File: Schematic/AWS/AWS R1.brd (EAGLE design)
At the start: 50 x 70 mm, 23 parts, among them U1 SN754410_NE_16

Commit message: Modified Board
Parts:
- added U$3: PTC, GeekAmmo:MC331XX
- moved J4 45.4 mm to (45.7, 58.4), flipped to the bottom
- moved J5 41.9 mm to (45.7, 48.3), flipped to the bottom
- moved J2 40.6 mm to (45.7, 27.9), flipped to the bottom
- moved J3 40.6 mm to (45.7, 17.8), flipped to the bottom
- moved J8 38.4 mm to (7.62, 27.9), flipped to the bottom
- moved J6 35.6 mm to (7.62, 61.0), flipped to the bottom
- moved D1 31.0 mm to (35.6, 58.4)
- moved R6 28.4 mm to (40.6, 25.4), turned to 270 degrees
- moved R8 25.9 mm to (15.2, 7.62), turned to 0 degrees
- moved R9 25.9 mm to (15.2, 10.2), turned to 0 degrees
- moved R1 25.4 mm to (12.7, 53.3)
- moved R2 20.5 mm to (15.2, 45.7), turned to 90 degrees
- moved C1 20.3 mm to (15.2, 62.2)
- moved D2 16.1 mm to (17.8, 50.8)
- moved R7 16.1 mm to (33.0, 17.8), turned to 0 degrees
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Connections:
- new net N$4: J4.1, U$3.P$2
- net 12V: now also U$3.P$1; no longer J4.1
- net 5V: now also J6.2; no longer J6.1
- net GND: now also J3.2, J6.1; no longer J3.1, J6.2
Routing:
- net A2: track 58.4 -> 3.59 mm
- net D1: track 30.5 -> 0.00 mm
- net D3: track 27.9 -> 5.08 mm
- net D6: track 0.00 -> 22.9 mm
- net GND: track 188.3 -> 173.0 mm
- net A1: track 2.54 -> 17.8 mm
- net A0: track 2.54 -> 17.8 mm
- net N$1: track 5.16 -> 17.9 mm
- net D4: track 12.7 -> 0.00 mm
- net A7: track 19.1 -> 7.62 mm
- net A6: track 10.2 -> 20.3 mm
- net N$4: track 0.00 -> 7.77 mm
- net SOL-: track 20.3 -> 15.2 mm
- net N$2: track 10.2 -> 7.62 mm
- net 12V: track 91.5 -> 89.0 mm
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
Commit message: final
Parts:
- moved R5 11.4 mm to (33.0, 15.2), turned to 180 degrees
- moved R6 9.16 mm to (35.6, 17.8), turned to 180 degrees
- moved R7 5.08 mm to (33.0, 12.7), flipped to the bottom
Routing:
- net GND: track 173.0 -> 216.2 mm
- net D3: track 5.08 -> 38.1 mm
- net 12V: track 89.0 -> 104.2 mm
- net N$2: track 7.62 -> 15.2 mm
- net D6: track 22.9 -> 27.9 mm
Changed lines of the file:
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@@
 <element name="R3" library="SparkFun-Resistors" package="AXIAL-0.4" value="10k" x="33.02" y="27.94" rot="R90"/>
 <element name="R4" library="SparkFun-Resistors" package="AXIAL-0.4" value="3.3k" x="30.48" y="30.48" rot="R270"/>
-<element name="R5" library="SparkFun-Resistors" package="AXIAL-0.4" value="10k" x="38.1" y="25.4" rot="R270"/>
-<element name="R6" library="SparkFun-Resistors" package="AXIAL-0.4" value="10k" x="40.64" y="25.4" rot="R270"/>
-<element name="R7" library="SparkFun-Resistors" package="AXIAL-0.4" value="3.3k" x="33.02" y="17.78"/>
+<element name="R5" library="SparkFun-Resistors" package="AXIAL-0.4" value="10k" x="33.02" y="15.24" rot="R180"/>
+<element name="R6" library="SparkFun-Resistors" package="AXIAL-0.4" value="10k" x="35.56" y="17.78" rot="R180"/>
+<element name="R7" library="SparkFun-Resistors" package="AXIAL-0.4" value="3.3k" x="33.02" y="12.7" rot="MR0"/>
 <element name="R8" library="SparkFun-Resistors" package="AXIAL-0.4" value="330" x="15.24" y="7.62"/>
 <element name="R9" library="SparkFun-Resistors" package="AXIAL-0.4" value="56k" x="15.24" y="10.16"/>
@@
 <wire x1="40.64" y1="50.8" x2="40.64" y2="53.34" width="0.4064" layer="1"/>
 <wire x1="40.64" y1="53.34" x2="38.1" y2="53.34" width="0.4064" layer="1"/>
-<wire x1="38.1" y1="30.48" x2="38.1" y2="33.02" width="0.4064" layer="1"/>
+<wire x1="38.1" y1="15.24" x2="38.1" y2="33.02" width="0.4064" layer="1"/>
 </signal>
 <signal name="GND">
@@
 <wire x1="22.86" y1="45.72" x2="20.32" y2="45.72" width="0.4064" layer="1"/>
 <wire x1="20.32" y1="48.26" x2="22.86" y2="48.26" width="0.4064" layer="1"/>
-<wire x1="48.26" y1="53.34" x2="48.26" y2="38.1" width="0.4064" layer="1"/>
+<wire x1="48.26" y1="53.34" x2="48.26" y2="45.72" width="0.4064" layer="1"/>
+<wire x1="48.26" y1="45.72" x2="48.26" y2="38.1" width="0.4064" layer="1"/>
 <wire x1="48.26" y1="38.1" x2="35.56" y2="38.1" width="0.4064" layer="1"/>
 <wire x1="35.56" y1="38.1" x2="35.56" y2="35.56" width="0.4064" layer="1"/>
@@
 <wire x1="20.32" y1="45.72" x2="17.78" y2="45.72" width="0.4064" layer="1"/>
 <wire x1="30.48" y1="35.56" x2="35.56" y2="35.56" width="0.4064" layer="1"/>
-<wire x1="48.26" y1="17.78" x2="48.26" y2="38.1" width="0.4064" layer="1"/>
+<wire x1="48.26" y1="22.86" x2="48.26" y2="38.1" width="0.4064" layer="1"/>
 <contactref element="J3" pad="2"/>
+<wire x1="48.26" y1="22.86" x2="45.72" y2="22.86" width="0.4064" layer="1"/>
+<wire x1="45.72" y1="22.86" x2="45.72" y2="22.78" width="0.4064" layer="1"/>
+<wire x1="38.1" y1="12.7" x2="48.26" y2="12.7" width="0.4064" layer="1"/>
+<wire x1="48.26" y1="12.7" x2="48.26" y2="22.86" width="0.4064" layer="1"/>
+<wire x1="27.94" y1="45.72" x2="27.94" y2="48.26" width="0.4064" layer="1"/>
+<wire x1="27.94" y1="48.26" x2="40.64" y2="48.26" width="0.4064" layer="1"/>
+<wire x1="40.64" y1="48.26" x2="40.64" y2="45.72" width="0.4064" layer="1"/>
+<wire x1="40.64" y1="45.72" x2="48.26" y2="45.72" width="0.4064" layer="1"/>
 <wire x1="48.26" y1="38.1" x2="45.72" y2="38.18" width="0" layer="19" extent="1-1"/>
 <wire x1="17.78" y1="63.5" x2="22.86" y2="63.5" width="0" layer="19" extent="1-16"/>
 <wire x1="15.24" y1="63.5" x2="17.78" y2="63.5" width="0" layer="19" extent="16-16"/>
-<wire x1="27.94" y1="48.26" x2="22.86" y2="48.26" width="0" layer="19" extent="1-1"/>
-<wire x1="27.94" y1="45.72" x2="27.94" y2="48.26" width="0" layer="19" extent="1-1"/>
-<wire x1="45.72" y1="22.78" x2="48.26" y2="17.78" width="0" layer="19" extent="1-1"/>
-<wire x1="27.94" y1="17.78" x2="30.48" y2="35.56" width="0" layer="19" extent="1-1"/>
-<wire x1="27.94" y1="5.08" x2="27.94" y2="17.78" width="0" layer="19" extent="1-1"/>
+<wire x1="27.94" y1="5.08" x2="38.1" y2="12.7" width="0" layer="19" extent="1-1"/>
 </signal>
 <signal name="5V">
@@
 <contactref element="R7" pad="P$2"/>
 <contactref element="U$1" pad="D3"/>
-<wire x1="15.24" y1="30.48" x2="38.1" y2="17.78" width="0" layer="19" extent="1-1"/>
-<wire x1="40.64" y1="20.32" x2="38.1" y2="20.32" width="0.4064" layer="1"/>
-<wire x1="38.1" y1="20.32" x2="38.1" y2="17.78" width="0.4064" layer="1"/>
+<wire x1="30.48" y1="17.78" x2="27.94" y2="17.78" width="0.4064" layer="1"/>
+<wire x1="27.94" y1="17.78" x2="27.94" y2="15.24" width="0.4064" layer="1"/>
+<wire x1="27.94" y1="15.24" x2="27.94" y2="12.7" width="0.4064" layer="1"/>
+<wire x1="27.94" y1="12.7" x2="17.78" y2="12.7" width="0.4064" layer="1"/>
+<wire x1="17.78" y1="12.7" x2="17.78" y2="30.48" width="0.4064" layer="1"/>
+<wire x1="17.78" y1="30.48" x2="15.24" y2="30.48" width="0.4064" layer="1"/>
 </signal>
 <signal name="D4">
@@
 <contactref element="U$1" pad="D6"/>
 <wire x1="20.32" y1="40.64" x2="17.78" y2="40.64" width="0.4064" layer="1"/>
-<wire x1="17.78" y1="40.64" x2="17.78" y2="22.86" width="0.4064" layer="1"/>
-<wire x1="17.78" y1="22.86" x2="15.24" y2="22.86" width="0.4064" layer="1"/>
+<wire x1="17.78" y1="40.64" x2="17.78" y2="38.1" width="0.4064" layer="1"/>
+<wire x1="17.78" y1="38.1" x2="12.7" y2="38.1" width="0.4064" layer="1"/>
+<wire x1="12.7" y1="38.1" x2="12.7" y2="22.86" width="0.4064" layer="1"/>
+<wire x1="12.7" y1="22.86" x2="15.24" y2="22.86" width="0.4064" layer="1"/>
 </signal>
 <signal name="A0">
@@
 <contactref element="R6" pad="P$1"/>
 <contactref element="J2" pad="1"/>
-<wire x1="40.64" y1="30.48" x2="45.72" y2="30.48" width="0.4064" layer="1"/>
-<wire x1="45.72" y1="30.48" x2="45.72" y2="27.94" width="0.4064" layer="1"/>
+<wire x1="45.72" y1="30.48" x2="45.72" y2="27.94" width="0" layer="19" extent="1-16"/>
+<wire x1="40.64" y1="17.78" x2="40.64" y2="27.94" width="0.4064" layer="1"/>
+<wire x1="40.64" y1="27.94" x2="45.72" y2="27.94" width="0.4064" layer="1"/>
 </signal>
 <signal name="D7">

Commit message: Moved outside
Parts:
- added J9: (no value), SparkFun-Connectors:SCREWTERMINAL-5MM-2
- R9: value 56k -> 51K
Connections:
- new net D0: J9.2, U$1.D0
- net A6: now also J9.1
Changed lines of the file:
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@@
 <element name="R7" library="SparkFun-Resistors" package="AXIAL-0.4" value="3.3k" x="33.02" y="12.7" rot="MR0"/>
 <element name="R8" library="SparkFun-Resistors" package="AXIAL-0.4" value="330" x="15.24" y="7.62"/>
-<element name="R9" library="SparkFun-Resistors" package="AXIAL-0.4" value="56k" x="15.24" y="10.16"/>
+<element name="R9" library="SparkFun-Resistors" package="AXIAL-0.4" value="51K" x="15.24" y="10.16"/>
 <element name="U$1" library="MoteinoR4Mod" package="MOTEINTO_R4_SQ" value="MOTEINO_R4_MODULEUSING_SQ_POST_PINS" x="25.4" y="20.32" rot="R270"/>
 <element name="U1" library="SN754410" package="NE16" value="SN754410_NE_16" x="27.94" y="38.1">
@@
 </element>
 <element name="U$3" library="GeekAmmo" package="MC331XX" value="PTC" x="38.1" y="53.34" rot="R90"/>
+<element name="J9" library="SparkFun-Connectors" package="SCREWTERMINAL-5MM-2" value="" x="5.08" y="-7.62">
+<attribute name="STOREFRONT_ID" value="PRT-08432" x="5.08" y="-7.62" size="1.778" layer="27" display="off"/>
+</element>
 </elements>
 <signals>
@@
 <contactref element="R9" pad="P$1"/>
 <contactref element="J8" pad="1"/>
-<wire x1="35.56" y1="20.32" x2="7.62" y2="27.94" width="0" layer="19" extent="1-1"/>
 <wire x1="10.16" y1="10.16" x2="10.16" y2="27.94" width="0.4064" layer="1"/>
 <wire x1="10.16" y1="27.94" x2="7.62" y2="27.94" width="0.4064" layer="1"/>
+<contactref element="J9" pad="1"/>
+<wire x1="10.16" y1="27.94" x2="35.56" y2="20.32" width="0" layer="19" extent="1-1"/>
+<wire x1="5.08" y1="-7.62" x2="10.16" y2="10.16" width="0" layer="19" extent="1-1"/>
 </signal>
 <signal name="A2">
@@
 <wire x1="45.72" y1="58.57" x2="45.72" y2="58.42" width="0.4064" layer="1"/>
 </signal>
+<signal name="D0">
+<contactref element="J9" pad="2"/>
+<contactref element="U$1" pad="D0"/>
+<wire x1="10.08" y1="-7.62" x2="35.56" y2="25.4" width="0" layer="19" extent="1-1"/>
+</signal>
 </signals>

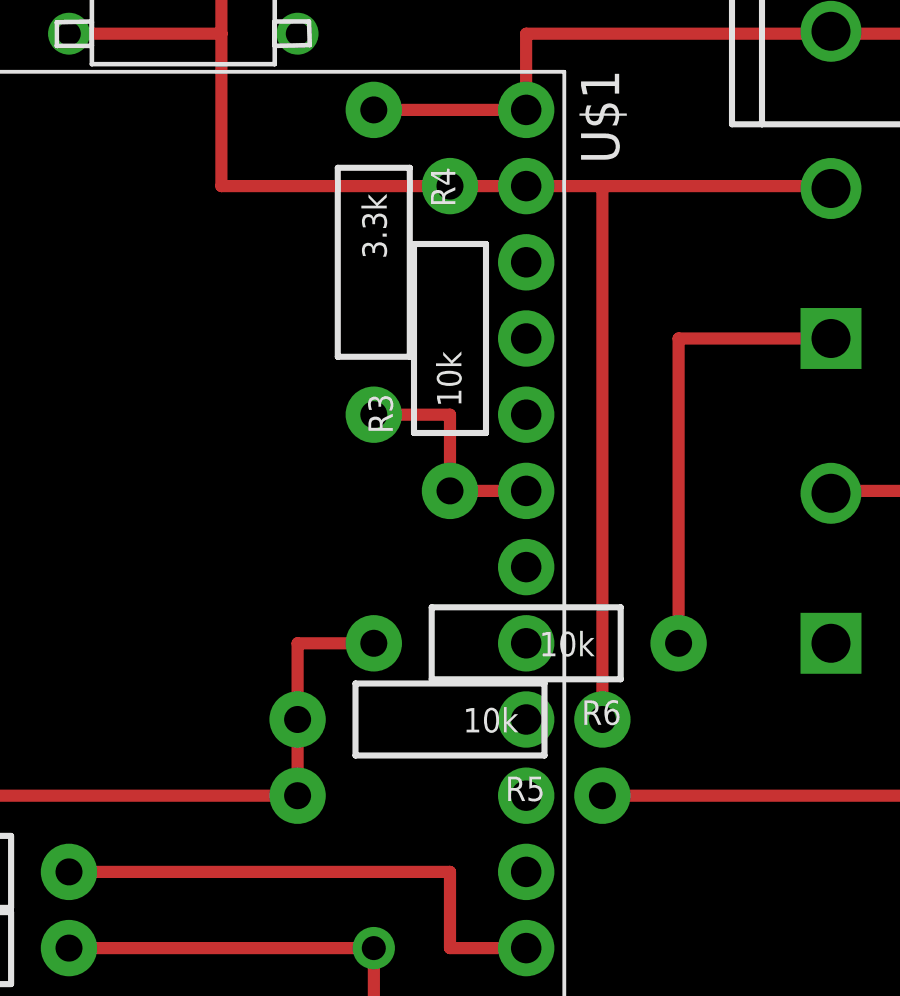
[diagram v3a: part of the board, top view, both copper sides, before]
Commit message: Removed 10k pullup on flow sensor
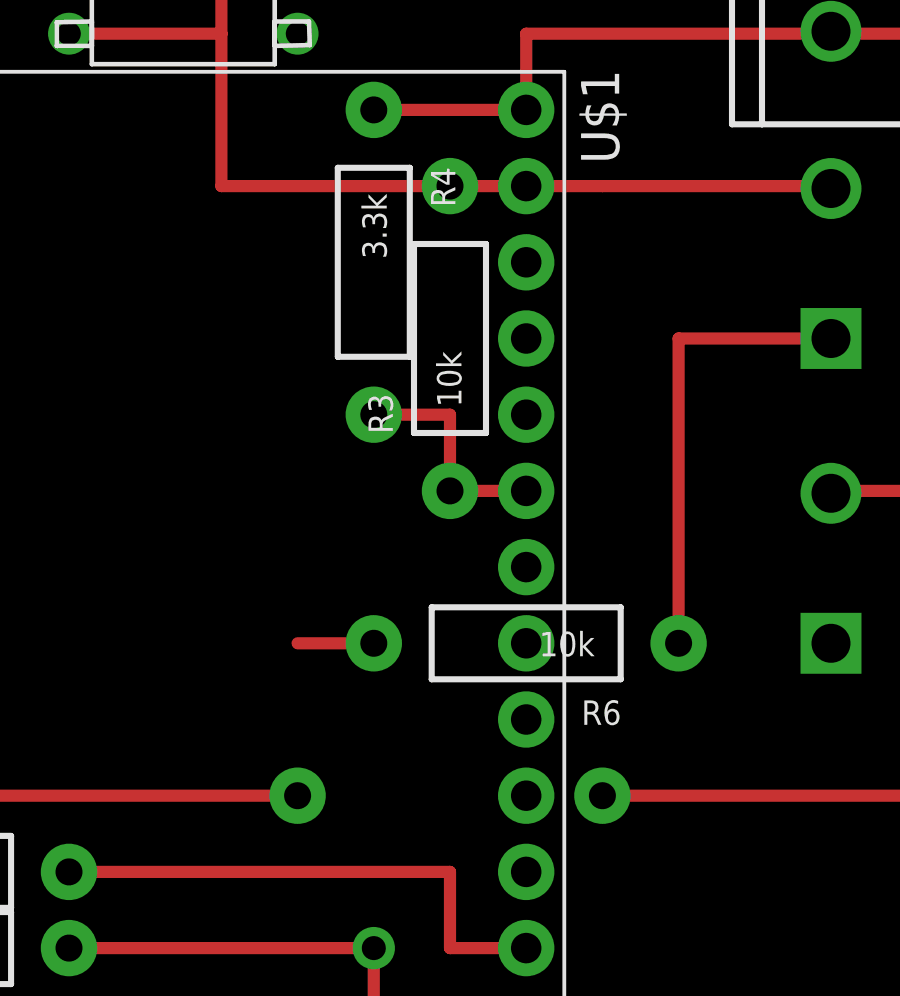
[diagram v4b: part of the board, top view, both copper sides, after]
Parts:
- removed R5: 10k, SparkFun-Resistors:AXIAL-0.4
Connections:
- net 12V: no longer R5.P$1
- net D3: no longer R5.P$2
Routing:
- net 12V: track 104.2 -> 86.4 mm
- net D3: track 38.1 -> 33.0 mm
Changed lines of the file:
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@@
 <element name="R3" library="SparkFun-Resistors" package="AXIAL-0.4" value="10k" x="33.02" y="27.94" rot="R90"/>
 <element name="R4" library="SparkFun-Resistors" package="AXIAL-0.4" value="3.3k" x="30.48" y="30.48" rot="R270"/>
-<element name="R5" library="SparkFun-Resistors" package="AXIAL-0.4" value="10k" x="33.02" y="15.24" rot="R180"/>
 <element name="R6" library="SparkFun-Resistors" package="AXIAL-0.4" value="10k" x="35.56" y="17.78" rot="R180"/>
 <element name="R7" library="SparkFun-Resistors" package="AXIAL-0.4" value="3.3k" x="33.02" y="12.7" rot="MR0"/>
@@
 <contactref element="C2" pad="1"/>
 <contactref element="U1" pad="8"/>
-<contactref element="R5" pad="P$1"/>
 <contactref element="J2" pad="2"/>
 <contactref element="U$3" pad="P$1"/>
@@
 <wire x1="40.64" y1="50.8" x2="40.64" y2="53.34" width="0.4064" layer="1"/>
 <wire x1="40.64" y1="53.34" x2="38.1" y2="53.34" width="0.4064" layer="1"/>
-<wire x1="38.1" y1="15.24" x2="38.1" y2="33.02" width="0.4064" layer="1"/>
 </signal>
 <signal name="GND">
@@
 <signal name="D3">
 <contactref element="R6" pad="P$2"/>
-<contactref element="R5" pad="P$2"/>
 <contactref element="R7" pad="P$2"/>
 <contactref element="U$1" pad="D3"/>
 <wire x1="30.48" y1="17.78" x2="27.94" y2="17.78" width="0.4064" layer="1"/>
-<wire x1="27.94" y1="17.78" x2="27.94" y2="15.24" width="0.4064" layer="1"/>
-<wire x1="27.94" y1="15.24" x2="27.94" y2="12.7" width="0.4064" layer="1"/>
 <wire x1="27.94" y1="12.7" x2="17.78" y2="12.7" width="0.4064" layer="1"/>
 <wire x1="17.78" y1="12.7" x2="17.78" y2="30.48" width="0.4064" layer="1"/>
 <wire x1="17.78" y1="30.48" x2="15.24" y2="30.48" width="0.4064" layer="1"/>
+<wire x1="27.94" y1="12.7" x2="27.94" y2="17.78" width="0" layer="19" extent="1-1"/>
 </signal>
 <signal name="D4">
